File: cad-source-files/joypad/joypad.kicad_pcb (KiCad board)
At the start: 2 copper layers, 174.5 x 80.6 mm, 82 parts, among them J2 ftdi_conn, J4 Conn_01x04, J5 Conn_01x04, SW1 SW_Push, SW10 SW_Push, SW11 SW_Push, SW12 SW_Push, SW2 SW_Push, SW3 SW_Push, SW4 SW_Push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

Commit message: jerry!
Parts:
- removed C1, C4: .1uF 100V, Capacitor_SMD:C_0805_2012Metric
- removed C14, C2, C5: .1uF, Capacitor_SMD:C_0603_1608Metric
- removed C15, C6: 22uF, Capacitor_SMD:C_0805_2012Metric
- removed C3: 4.7uF 100V, Capacitor_SMD:C_0805_2012Metric
- removed D7: D_TVS_x2_AAC, Package_TO_SOT_SMD:SOT-23
- removed H10, H11, H6, H7, H8, H9: MountingHole, MountingHole:MountingHole_2.5mm_Pad
- removed J4, J5: Conn_01x04, Connector_JST:JST_PH_S4B-PH-SM4-TB_1x04-1MP_P2.00mm_Horizontal
- removed L1: 22uH, EvezorLIB:INDUCTOR_7.5X6.6_GCDA0630-220MC
- removed R1: 10k, Resistor_SMD:R_0603_1608Metric
- removed R2: 82k, Resistor_SMD:R_0603_1608Metric
- removed TP1, TP10, TP2, TP3, TP4, TP5, TP6, TP7, TP8, TP9: TestPoint, Evezor_extras:TestPoint_THTPad_D1.0mm_Drill0.5mm
- removed U1: SY8401ABC, Package_TO_SOT_SMD:SOT-23-6
- removed U5: Trans_CAN_SN65HVD230DR, EvezorLIB:CAN-TRANS-SN65HVD230DR
- added J1: Conn_01x04, Connector_PinSocket_2.54mm:PinSocket_1x04_P2.54mm_Vertical, F.Cu at (133.1, 67.5)
- added J3: Barrel_Jack, Connector_BarrelJack:BarrelJack_Horizontal, F.Cu at (162.2, 79.8)
- J2: footprint Evezor_extras:CONN-SH-6P-VERTICAL -> Connector_JST:JST_SH_SM06B-SRSS-TB_1x06-1MP_P1.00mm_Horizontal
- SW1, SW11, SW12, SW2, SW3, SW4, SW5, SW6: footprint EvezorLIB:SWITCH_2x3_SMD_TACTILE_GREEN -> Button_Switch_SMD:SWITCH_2x3_SMD_TACTILE_GREEN
- U3: footprint Evezor_extras:ESP32-WROOM-32U -> RF_Module:ESP32-WROOM-32U_evezor
- moved D8 57.9 mm to (88.8, 80.3), turned to -90 degrees
- moved R7 57.6 mm to (92.1, 79.5)
- moved SW2 55.6 mm to (96.2, 76.0), turned to 180 degrees
- moved C7 52.2 mm to (100.8, 68.6), turned to 180 degrees
- moved R6 48.1 mm to (101.7, 71.5)
- moved D1 47.9 mm to (113.7, 97.1), turned to 0 degrees
- moved U2 47.6 mm to (105.3, 94.0), turned to 90 degrees
- moved C11 44.8 mm to (105.1, 69.6), turned to -90 degrees
- moved C10 42.0 mm to (104.5, 85.8)
- moved C13 40.1 mm to (106.2, 88.0), turned to 0 degrees
- moved D2 36.8 mm to (113.7, 91.6), turned to 0 degrees
- moved SW1 31.8 mm to (140.1, 108.1), turned to 0 degrees
- moved J2 30.6 mm to (148.2, 69.0), turned to 180 degrees
- moved D6 30.4 mm to (130.3, 107.7)
- moved C9 26.0 mm to (131.8, 103.9), turned to 0 degrees
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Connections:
- D1 pad 1: Net-(C1-Pad1) -> Net-(U2-Pad3)
- D1 pad 2: GND -> VBUS
- D2 pad 1: /PWR -> Net-(U2-Pad3)
- D2 pad 2: VBUS -> +5V
- D8 pad 2: /PWR -> +3V3
- J2 pad 5: VBUS -> +5V
- U2 pad 3: /VREG_OUT -> Net-(U2-Pad3)
- U3 pad 10: /GREEN -> unconnected-(U3-Pad10)
- U3 pad 11: /RED -> unconnected-(U3-Pad11)
- U3 pad 12: /BLUE -> unconnected-(U3-Pad12)
- U3 pad 13: /JOY_SW_2 -> unconnected-(U3-Pad13)
- U3 pad 14: /NEO_BAR -> unconnected-(U3-Pad14)
- U3 pad 16: /START -> unconnected-(U3-Pad16)
- U3 pad 23: /SELECT -> unconnected-(U3-Pad23)
- U3 pad 24: /CAN_SLP -> unconnected-(U3-Pad24)
- U3 pad 26: /CAN_TX -> unconnected-(U3-Pad26)
- U3 pad 27: /CAN_RX -> unconnected-(U3-Pad27)
- U3 pad 28: /NEO_STATUS -> unconnected-(U3-Pad28)
- U3 pad 29: /HBT_LED -> unconnected-(U3-Pad29)
- U3 pad 30: /JOY_SW_1 -> unconnected-(U3-Pad30)
- U3 pad 31: /LEFT -> unconnected-(U3-Pad31)
- U3 pad 33: /UP -> unconnected-(U3-Pad33)
- U3 pad 36: /RIGHT -> unconnected-(U3-Pad36)
- U3 pad 37: /DOWN -> unconnected-(U3-Pad37)
- U3 pad 9: /YELLOW -> unconnected-(U3-Pad9)
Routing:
- net +3V3: track 236.0 -> 105.4 mm, vias 5 -> 0
- net /RED: track 94.8 -> 0.00 mm, vias 2 -> 0
- net /YELLOW: track 86.9 -> 0.00 mm, vias 2 -> 0
- net /START: track 80.3 -> 0.00 mm
- net /BLUE: track 79.9 -> 0.00 mm, vias 2 -> 0
- net /GREEN: track 74.1 -> 0.00 mm, vias 2 -> 0
- net /JOY_SW_2: track 71.5 -> 6.50 mm
- net /JOY_SW_1: track 64.4 -> 0.00 mm, vias 2 -> 0
- net /LEFT: track 61.6 -> 0.00 mm, vias 2 -> 0
- net /SELECT: track 60.5 -> 0.00 mm
- net /JOY_X_1: track 60.1 -> 0.00 mm, vias 2 -> 0
- net /JOY_Y_2: track 59.0 -> 0.00 mm
- net /DOWN: track 53.6 -> 0.00 mm
- net /JOY_Y_1: track 50.9 -> 0.00 mm, vias 2 -> 0
- net /UP: track 45.8 -> 0.00 mm, vias 2 -> 0
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- removed copper zone on F.Cu, net +3V3
- removed copper zone on F.Cu, net /VREG_OUT
- removed copper zone on F.Cu, net Net-(C1-Pad1)
- removed copper zone on B.Cu, net VBUS
- removed copper zone on F.Cu, net VBUS
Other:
- board text removed: "3V"
- board text removed: "BOOT"
- board text removed: "FNC"
- board text removed: "G"
- board text removed: "H"
- board text removed: "RST"
- board text removed: "RX"
- board text removed: "TX"
- board text removed: "V+"
- board text removed: "VREG"

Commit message: things are connected but theres still more things to be done
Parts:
- moved D3 26.2 mm to (150.5, 108.1)
- moved R5 26.2 mm to (147.6, 108.9)
- moved C9 4.65 mm to (127.1, 104.0)
- moved D6 4.19 mm to (126.1, 107.7)
- moved R3 4.17 mm to (130.7, 106.8)
- moved SW1 2.99 mm to (137.4, 106.8)
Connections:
- U3 pad 10: unconnected-(U3-Pad10) -> /LEFT
- U3 pad 11: unconnected-(U3-Pad11) -> /DOWN
- U3 pad 12: unconnected-(U3-Pad12) -> /UP
- U3 pad 13: unconnected-(U3-Pad13) -> /RIGHT
- U3 pad 14: unconnected-(U3-Pad14) -> /SELECT
- U3 pad 16: unconnected-(U3-Pad16) -> /NEO_STATUS
- U3 pad 23: unconnected-(U3-Pad23) -> /NEO_BAR
- U3 pad 24: unconnected-(U3-Pad24) -> /HBT_LED
- U3 pad 27: unconnected-(U3-Pad27) -> /START
- U3 pad 28: unconnected-(U3-Pad28) -> /JOY_SW_2
- U3 pad 29: unconnected-(U3-Pad29) -> /GREEN
- U3 pad 30: unconnected-(U3-Pad30) -> /BLUE
- U3 pad 31: unconnected-(U3-Pad31) -> /YELLOW
- U3 pad 33: unconnected-(U3-Pad33) -> /RED
- U3 pad 36: unconnected-(U3-Pad36) -> /LCD_SDA
- U3 pad 37: unconnected-(U3-Pad37) -> /LCD_SCL
- U3 pad 9: unconnected-(U3-Pad9) -> /JOY_SW_1
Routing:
- net +3V3: track 105.4 -> 230.4 mm, vias 0 -> 1
- net /START: track 0.00 -> 119.3 mm
- net /JOY_Y_2: track 0.00 -> 102.9 mm, vias 0 -> 2
- net /JOY_SW_2: track 6.50 -> 94.6 mm
- net /JOY_X_2: track 0.00 -> 86.7 mm, vias 0 -> 2
- net /YELLOW: track 0.00 -> 84.2 mm
- net /GREEN: track 0.00 -> 76.8 mm
- net /RESET: track 12.5 -> 88.2 mm, vias 0 -> 2
- net /RED: track 0.00 -> 70.3 mm
- net /NEO_BAR: track 0.00 -> 68.0 mm, vias 0 -> 2
- net /NEO_STATUS: track 0.00 -> 67.8 mm, vias 0 -> 2
- net /SELECT: track 0.00 -> 66.8 mm
- net /DOWN: track 0.00 -> 66.4 mm
- net /FUNCTION_BUTTON: track 0.00 -> 59.6 mm
- net /BLUE: track 0.00 -> 59.0 mm
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
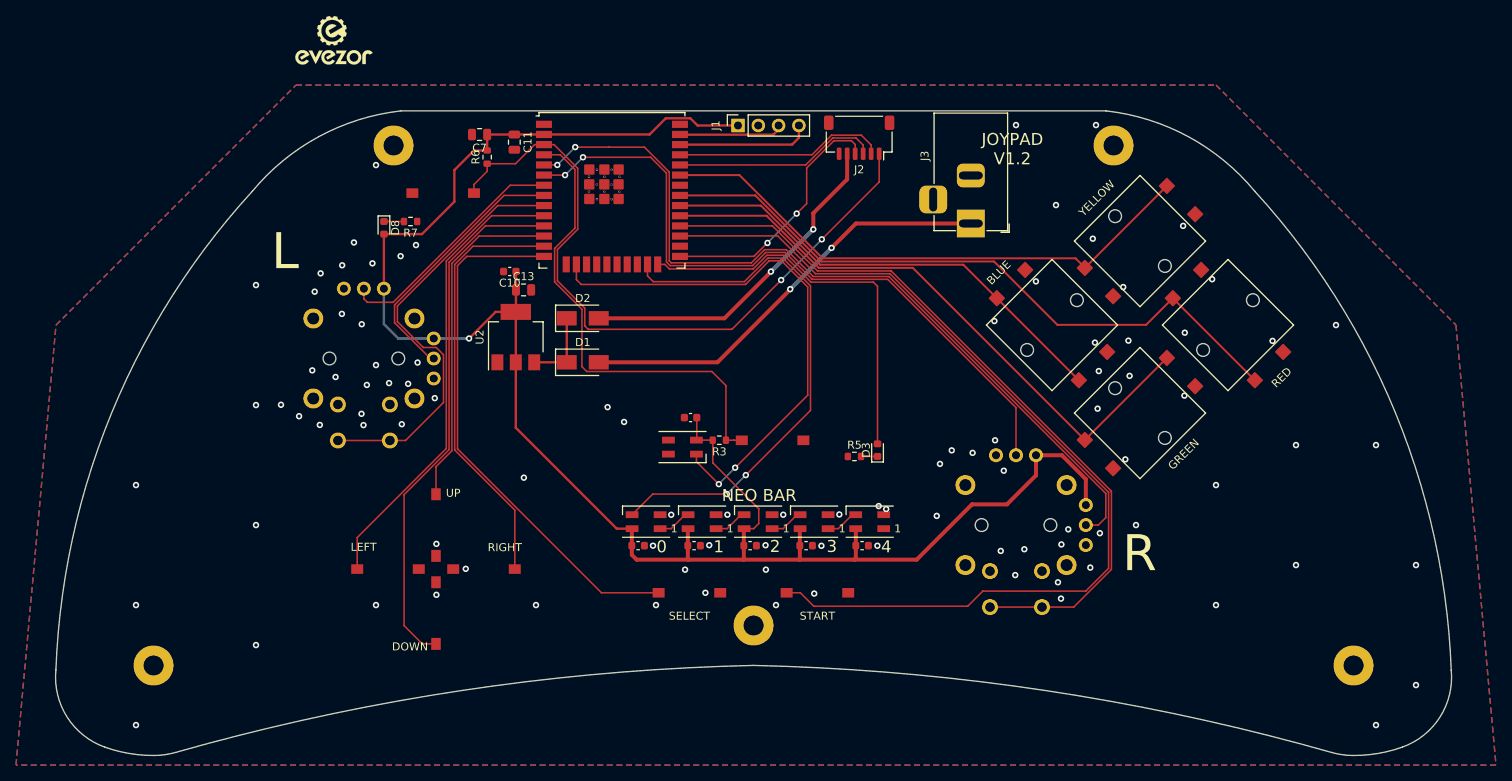
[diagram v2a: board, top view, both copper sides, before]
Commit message: ground pads were weird. All fixed :)
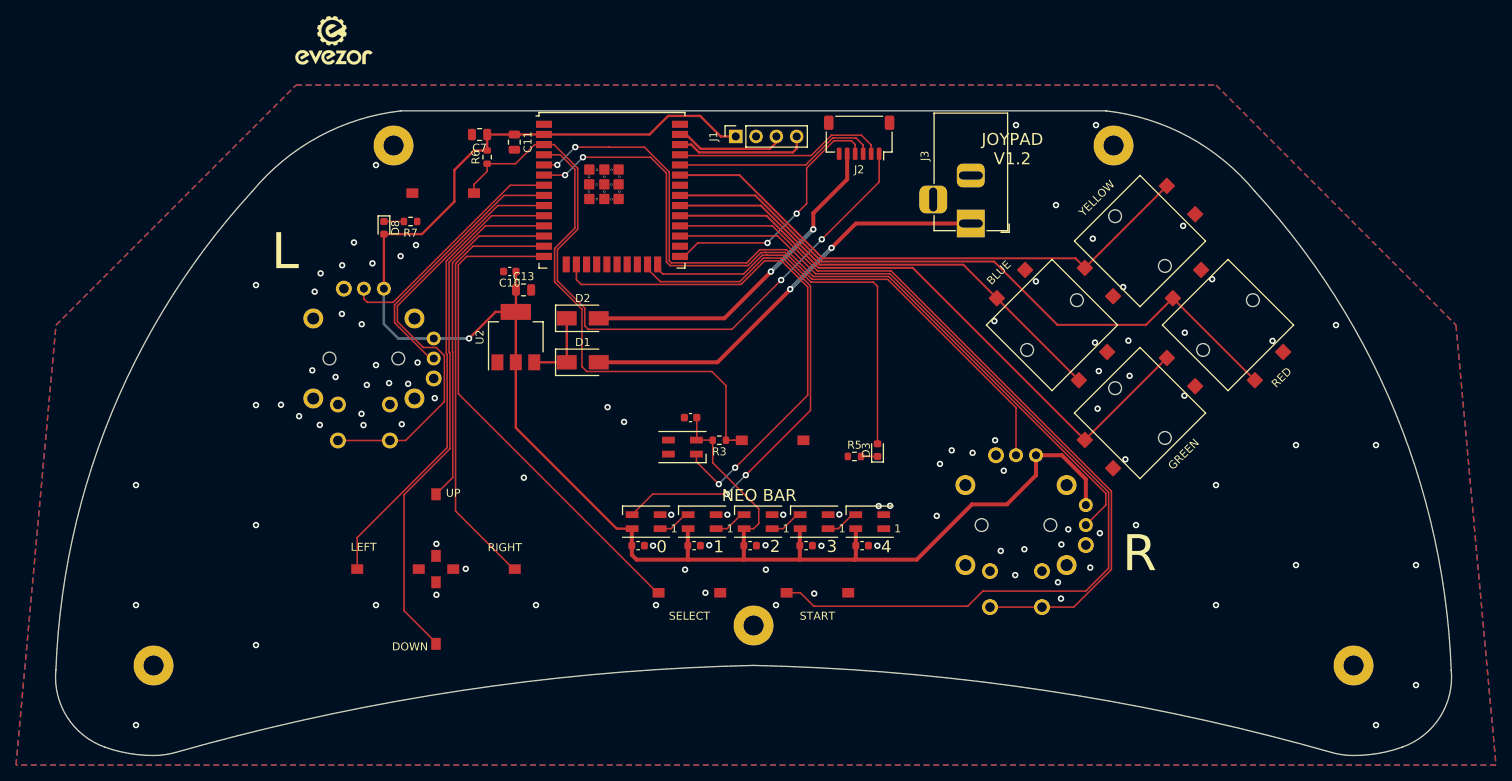
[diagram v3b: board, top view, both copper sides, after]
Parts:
- moved J1 1.40 mm to (132.8, 68.9)
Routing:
- net /SELECT: track 66.8 -> 62.6 mm
- net /JOY_Y_2: track 102.9 -> 101.9 mm
- net /DOWN: track 66.4 -> 65.5 mm
- net /HBT_LED: track 49.7 -> 50.6 mm
- net /LCD_SCL: track 13.1 -> 13.9 mm
- net +3V3: track 230.4 -> 230.9 mm
- net /NEO_BAR: track 68.0 -> 67.5 mm

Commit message: drawings and viass wooooooo
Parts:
- added ?: , clipboard:05d6695d-834d-4c2c-87ce-5d7e479e85e7, B.Cu at (175.0, 65.2)
- added G***: LOGO, Symbol:mustache man 2, F.Cu at (208.6, 121.8)
- added G***: LOGO, Symbol:mustache man, F.Cu at (115.6, 113.5)
- moved G*** 18.2 mm to (81.7, 73.9)
- moved G*** 18.2 mm to (82.0, 77.2)
- moved G*** 7.30 mm to (168.6, 83.6)
- moved REF** 6.61 mm to (168.7, 76.9)
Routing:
- net /SELECT: track 62.6 -> 66.5 mm
- net /RED: track 70.3 -> 72.4 mm
- net /RIGHT: track 53.3 -> 55.3 mm
- net /DOWN: track 65.5 -> 66.4 mm
- net /JOY_X_2: track 86.7 -> 87.5 mm
- net /UP: track 42.6 -> 43.3 mm
- net /HBT_LED: track 50.6 -> 50.0 mm
- net /BOOT: track 31.9 -> 32.5 mm
- net /YELLOW: track 84.2 -> 83.6 mm
- net GND: vias 99 -> 333
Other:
- board text added: "Carl V_1"
- board text added: "Made by Olivia & Andrew 2022"
- board text added: "https://github.com/Mechanical-Mustaches/mini_mustache"
- board text added: "taftrobotics8122.wixsite.com/mechanical-mustaches"

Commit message: nvm i wanted text in a different place
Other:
- board text added: "Carl the Controller"
- board text added: "V_1"
- board text removed: "Carl V_1"
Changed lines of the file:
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@@
     (effects (font (size 1.5 1.5) (thickness 0.35)) (justify mirror))
-  )
-  (gr_text "Carl V_1" (at 107.79 86.45) (layer "B.SilkS")
-    (effects (font (size 2.5 2.5) (thickness 0.625)) (justify mirror))
   )
   (gr_text "Made by Olivia & Andrew 2022" (at 141.83 81.06) (layer "B.SilkS")
@@
     (effects (font (size 1.5 1.5) (thickness 0.3)))
   )
+  (gr_text "V_1" (at 134.6 101.24) (layer "F.SilkS")
+    (effects (font (size 2.5 2.5) (thickness 0.625)))
+  )
   (gr_text "UP\n" (at 97.454652 113.446558) (layer "F.SilkS")
     (effects (font (size 1 1) (thickness 0.25)))
@@
     (effects (font (size 1 1) (thickness 0.25)))
   )
+  (gr_text "Carl the Controller " (at 137.3 96.56) (layer "F.SilkS")
+    (effects (font (size 2.5 2.5) (thickness 0.625)))
+  )
   (gr_text "START" (at 142.98 128.81) (layer "F.SilkS")

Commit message: okok thisss time cause now it has a mustachey logo
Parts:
- added G***: LOGO, Symbol:Mustache20mm, F.Cu at (135.5, 98.8)
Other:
- board text added: "Carl V_1"
- board text removed: "Carl the Controller"
- board text removed: "V_1"

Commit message: 12-2 boards ordered
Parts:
- removed the G*** at (81.7, 73.9)
- removed the G*** at (82.0, 77.2)
- G***: footprint Symbol:Mustache20mm -> Symbol:mustache_logo_25mm
- SW10, SW7, SW8, SW9: footprint Evezor_BUTTONS:12mm_pushbutton -> Button_Switch_SMD:12mm_pushbutton
- U4, U6: footprint Evezor_BUTTONS:JOYSTICK -> Potentiometer_THT:JOYSTICK
- moved G*** 6.88 mm to (133.9, 92.2)
- moved D3 5.00 mm to (146.2, 105.6), turned to 0 degrees
- moved R5 1.90 mm to (146.1, 107.7), turned to 180 degrees
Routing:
- net GND: vias 333 -> 331
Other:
- board text added: "JOYPAD V1.1"
- board text added: "Joypad V1.1"
- board text added: "PWR LED"
- board text added: "RESET"
- board text added: "function button"
- board text added: "hbt"
- board text added: "nemo"
- board text added: "stache station"
- board text added: "status"
- board text removed: "Carl V_1"
- board text removed: "JOYPAD V1.2"
- board text removed: "NEO BAR"
